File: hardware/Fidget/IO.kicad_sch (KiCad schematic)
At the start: 16 parts

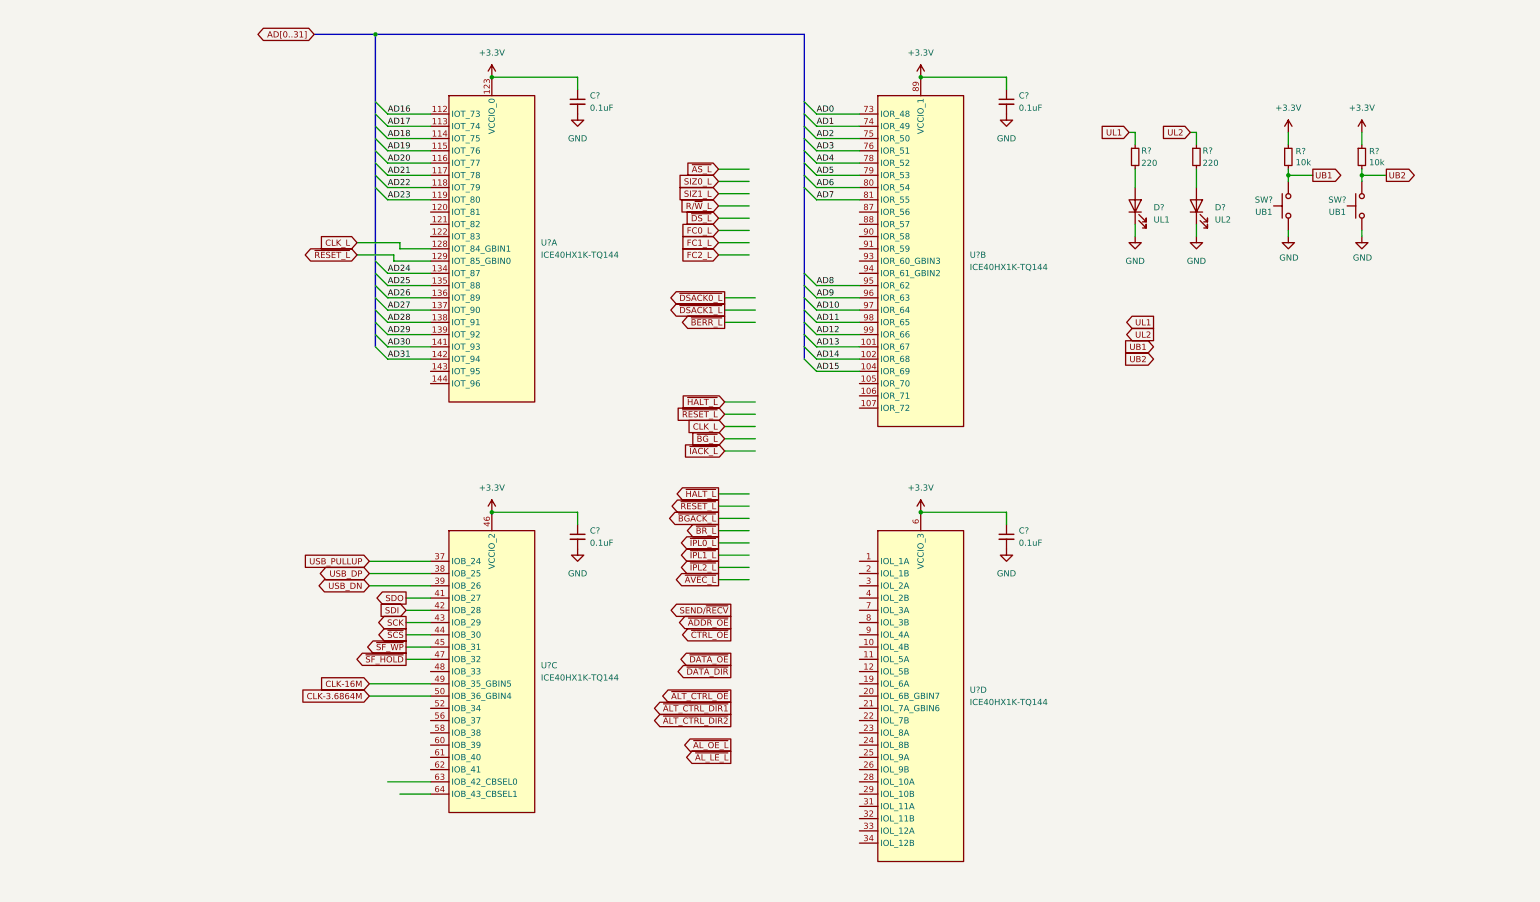
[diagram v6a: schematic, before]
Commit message: Minor updates, and start of PCB layout
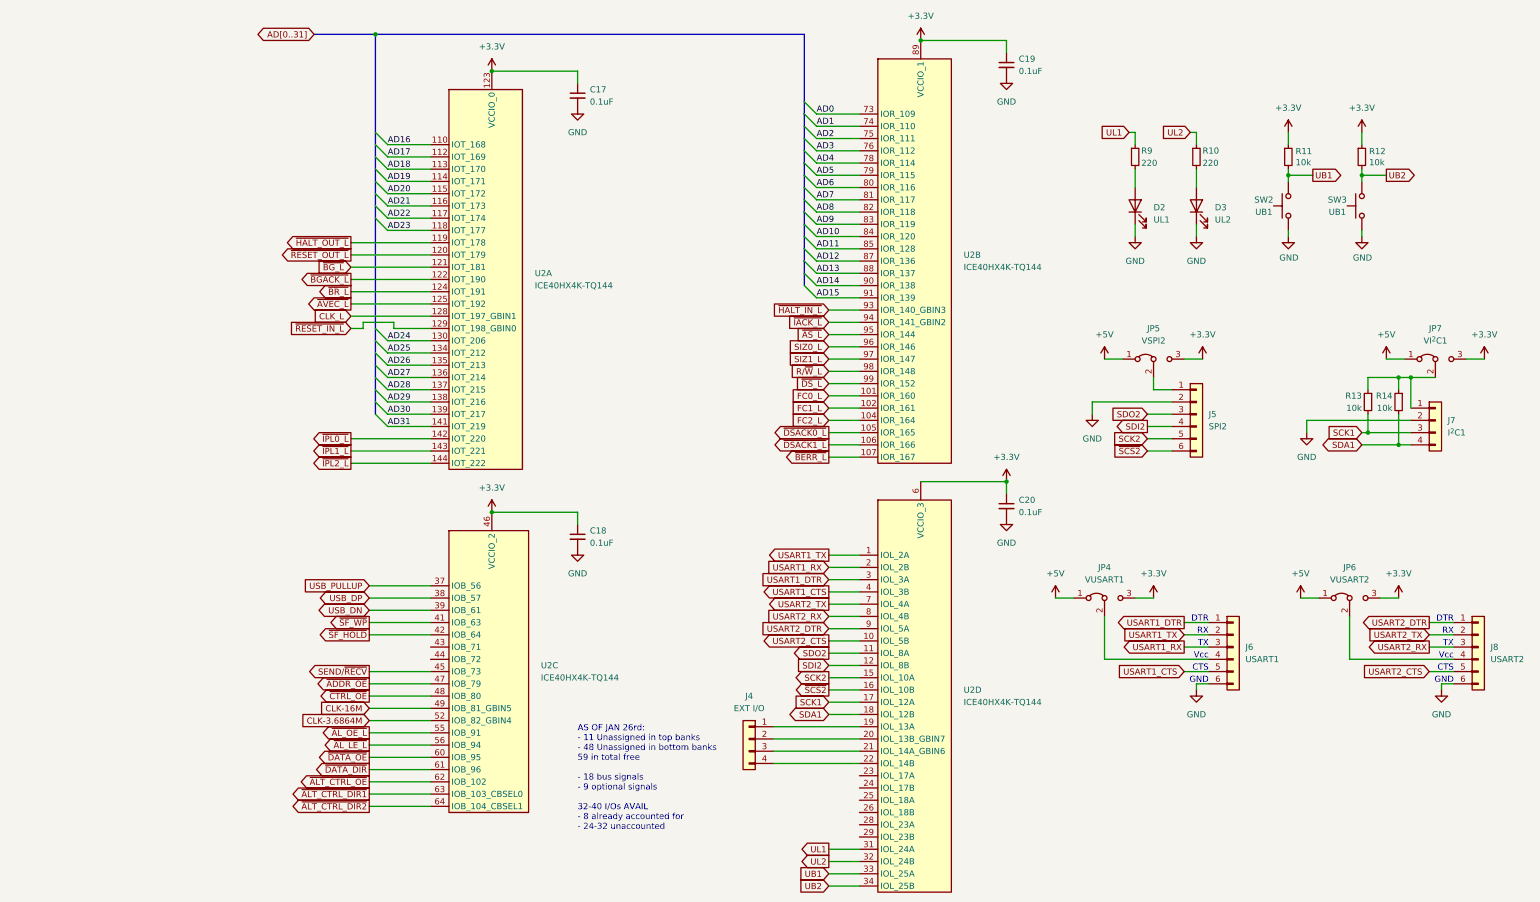
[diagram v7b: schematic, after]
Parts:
- removed U? (x4): ICE40HX1K-TQ144, Package_QFP:TQFP-144_20x20mm_P0.5mm, symbol FPGA_Lattice:ICE40HX1K-TQ144
- added J4: EXT I/O, Connector_PinHeader_2.54mm:PinHeader_1x04_P2.54mm_Vertical, symbol Connector_Generic:Conn_01x04
- added J5: SPI2, Connector_PinHeader_2.54mm:PinHeader_1x06_P2.54mm_Vertical, symbol Connector_Generic:Conn_01x06
- added J6: USART1, Connector_PinHeader_2.54mm:PinHeader_1x06_P2.54mm_Vertical, symbol Connector_Generic:Conn_01x06
- added J7: I^{2}C1, Connector_PinHeader_2.54mm:PinHeader_1x04_P2.54mm_Vertical, symbol Connector_Generic:Conn_01x04
- added J8: USART2, Connector_PinHeader_2.54mm:PinHeader_1x06_P2.54mm_Vertical, symbol Connector_Generic:Conn_01x06
- added JP4: VUSART1, Connector_PinHeader_2.54mm:PinHeader_1x03_P2.54mm_Vertical, symbol Jumper:Jumper_3_Bridged12
- added JP5: VSPI2, Connector_PinHeader_2.54mm:PinHeader_1x03_P2.54mm_Vertical, symbol Jumper:Jumper_3_Bridged12
- added JP6: VUSART2, Connector_PinHeader_2.54mm:PinHeader_1x03_P2.54mm_Vertical, symbol Jumper:Jumper_3_Bridged12
- added JP7: VI^{2}C1, Connector_PinHeader_2.54mm:PinHeader_1x03_P2.54mm_Vertical, symbol Jumper:Jumper_3_Bridged12
- added R13, R14: 10k, Resistor_THT:R_Axial_DIN0204_L3.6mm_D1.6mm_P5.08mm_Horizontal, symbol Device:R_Small
- added U2: ICE40HX4K-TQ144, Package_QFP:TQFP-144_20x20mm_P0.5mm, symbol FPGA_Lattice:ICE40HX4K-TQ144
- C17, C18, C19, C20: renamed from C?; footprint (none) -> Capacitor_SMD:C_0805_2012Metric_Pad1.18x1.45mm_HandSolder
- R10, R9: renamed from R?; footprint (none) -> Resistor_THT:R_Axial_DIN0204_L3.6mm_D1.6mm_P5.08mm_Horizontal
- gave numbers to parts that had none: 6
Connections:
- net +3.3V: now also JP4.3 (B), JP5.3 (B), JP6.3 (B), JP7.3 (B), U2.100 (VCCIO_1), U2.123 (VCCIO_0), U2.131 (VCCIO_0), U2.30 (VCCIO_3), U2.46 (VCCIO_2), U2.57 (VCCIO_2), U2.6 (VCCIO_3), U2.89 (VCCIO_1)
- net AD0: now also U2.73 (IOR_109)
- net AD1: now also U2.74 (IOR_110)
- net AD10: now also U2.84 (IOR_120)
- net AD11: now also U2.85 (IOR_128)
- net AD12: now also U2.87 (IOR_136)
- net AD13: now also U2.88 (IOR_137)
- net AD14: now also U2.90 (IOR_138)
- net AD15: now also U2.91 (IOR_139)
- net AD16: now also U2.110 (IOT_168)
- net AD17: now also U2.112 (IOT_169)
- net AD18: now also U2.113 (IOT_170)
- net AD19: now also U2.114 (IOT_171)
- net AD2: now also U2.75 (IOR_111)
- net AD20: now also U2.115 (IOT_172)
- net AD21: now also U2.116 (IOT_173)
- net AD22: now also U2.117 (IOT_174)
- net AD23: now also U2.118 (IOT_177)
- net AD24: now also U2.130 (IOT_206)
- net AD25: now also U2.134 (IOT_212)
- net AD26: now also U2.135 (IOT_213)
- net AD27: now also U2.136 (IOT_214)
- net AD28: now also U2.137 (IOT_215)
- net AD29: now also U2.138 (IOT_216)
- net AD3: now also U2.76 (IOR_112)
- net AD30: now also U2.139 (IOT_217)
- net AD31: now also U2.141 (IOT_219)
- net AD4: now also U2.78 (IOR_114)
- net AD5: now also U2.79 (IOR_115)
- net AD6: now also U2.80 (IOR_116)
- net AD7: now also U2.81 (IOR_117)
- net AD8: now also U2.82 (IOR_118)
- net AD9: now also U2.83 (IOR_119)
- net CLK-16M: now also U2.49 (IOB_81_GBIN5)
- net CLK-3.6864M: now also U2.52 (IOB_82_GBIN4)
- net CLK_L: now also U2.128 (IOT_197_GBIN1)
- net FC0_L: now also U2.101 (IOR_160)
- net FC1_L: now also U2.102 (IOR_161)
- net FC2_L: now also U2.104 (IOR_164)
- net GND: now also J5.2 (Pin_2), J6.6 (Pin_6), J7.2 (Pin_2), J8.6 (Pin_6)
- net R/~{W}_L: now also U2.98 (IOR_148)
- net SEND/~{RECV}: now also U2.45 (IOB_73)
- net SIZ0_L: now also U2.96 (IOR_146)
- net SIZ1_L: now also U2.97 (IOR_147)
- net UB1: now also U2.33 (IOL_25A)
- net UB2: now also U2.34 (IOL_25B)
- net UL1: now also U2.31 (IOL_24A)
- net UL2: now also U2.32 (IOL_24B)
- net USB_DN: now also U2.39 (IOB_61)
- net USB_DP: now also U2.38 (IOB_57)
- net USB_PULLUP: now also U2.37 (IOB_56)
- net ~{ADDR_OE}: now also U2.47 (IOB_79)
- net ~{ALT_CTRL_DIR1}: now also U2.63 (IOB_103_CBSEL0)
- net ~{ALT_CTRL_DIR2}: now also U2.64 (IOB_104_CBSEL1)
- net ~{ALT_CTRL_OE}: now also U2.62 (IOB_102)
- net ~{AL_LE_L}: now also U2.56 (IOB_94)
- net ~{AL_OE_L}: now also U2.55 (IOB_91)
- net ~{AS_L}: now also U2.95 (IOR_144)
- net ~{AVEC_L}: now also U2.125 (IOT_192)
- net ~{BERR_L}: now also U2.107 (IOR_167)
- net ~{BGACK_L}: now also U2.122 (IOT_190)
- net ~{BG_L}: now also U2.121 (IOT_181)
- net ~{BR_L}: now also U2.124 (IOT_191)
- net ~{CTRL_OE}: now also U2.48 (IOB_80)
- net ~{DATA_DIR}: now also U2.61 (IOB_96)
- net ~{DATA_OE}: now also U2.60 (IOB_95)
- net ~{DSACK0_L}: now also U2.105 (IOR_165)
- net ~{DSACK1_L}: now also U2.106 (IOR_166)
- net ~{DS_L}: now also U2.99 (IOR_152)
- net ~{IACK_L}: now also U2.94 (IOR_141_GBIN2)
- net ~{IPL0_L}: now also U2.142 (IOT_220)
- net ~{IPL1_L}: now also U2.143 (IOT_221)
- net ~{IPL2_L}: now also U2.144 (IOT_222)
- net ~{SF_HOLD}: now also U2.42 (IOB_64)
- net ~{SF_WP}: now also U2.41 (IOB_63)
- new net: J5.1 (Pin_1), JP5.2 (C)
- new net: J6.4 (Pin_4), JP4.2 (C)
- new net: J4.1 (Pin_1), U2.19 (IOL_13A)
- new net: J4.2 (Pin_2), U2.20 (IOL_13B_GBIN7)
- new net: J4.3 (Pin_3), U2.21 (IOL_14A_GBIN6)
- new net: J4.4 (Pin_4), U2.22 (IOL_14B)
- new net: J8.4 (Pin_4), JP6.2 (C)
- new net: J7.1 (Pin_1), JP7.2 (C), R13.1, R14.1
- new net +5V: JP4.1 (A), JP5.1 (A), JP6.1 (A), JP7.1 (A)
- new net SCK1: J7.3 (Pin_3), R13.2, U2.17 (IOL_12A)
- new net SCK2: J5.5 (Pin_5), U2.15 (IOL_10A)
- new net SDA1: J7.4 (Pin_4), R14.2, U2.18 (IOL_12B)
- new net SDI2: J5.4 (Pin_4), U2.12 (IOL_8B)
- new net SDO2: J5.3 (Pin_3), U2.11 (IOL_8A)
- new net USART1_CTS: J6.5 (Pin_5), U2.4 (IOL_3B)
- new net USART1_DTR: J6.1 (Pin_1), U2.3 (IOL_3A)
- new net USART1_RX: J6.3 (Pin_3), U2.2 (IOL_2B)
- new net USART1_TX: J6.2 (Pin_2), U2.1 (IOL_2A)
- new net USART2_CTS: J8.5 (Pin_5), U2.10 (IOL_5B)
- new net USART2_DTR: J8.1 (Pin_1), U2.9 (IOL_5A)
- new net USART2_RX: J8.3 (Pin_3), U2.8 (IOL_4B)
- new net USART2_TX: J8.2 (Pin_2), U2.7 (IOL_4A)
- new net ~{HALT_IN_L}: U2.93 (IOR_140_GBIN3)
- new net ~{HALT_OUT_L}: U2.119 (IOT_178)
- new net ~{RESET_IN_L}: U2.129 (IOT_198_GBIN0)
- new net ~{RESET_OUT_L}: U2.120 (IOT_179)
- new net ~{SCS2}: J5.6 (Pin_6), U2.16 (IOL_10B)
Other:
- note added: "AS OF JAN 26rd: - 11 Unassigned in top banks - 48 Unassigned in bottom banks 59 in total free - 18 bus signals - 9 optional signals 32-40 I/Os AVAIL - 8 already accounted for - 24-32 unaccounted"
- note added: "CTS"
- note added: "DTR"
- note added: "GND"
- note added: "RX"
- note added: "TX"
- note added: "Vcc"
- moved on the sheet: C17, C19, C20

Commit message: More PCB layout and fixes and reassigments to the schematics
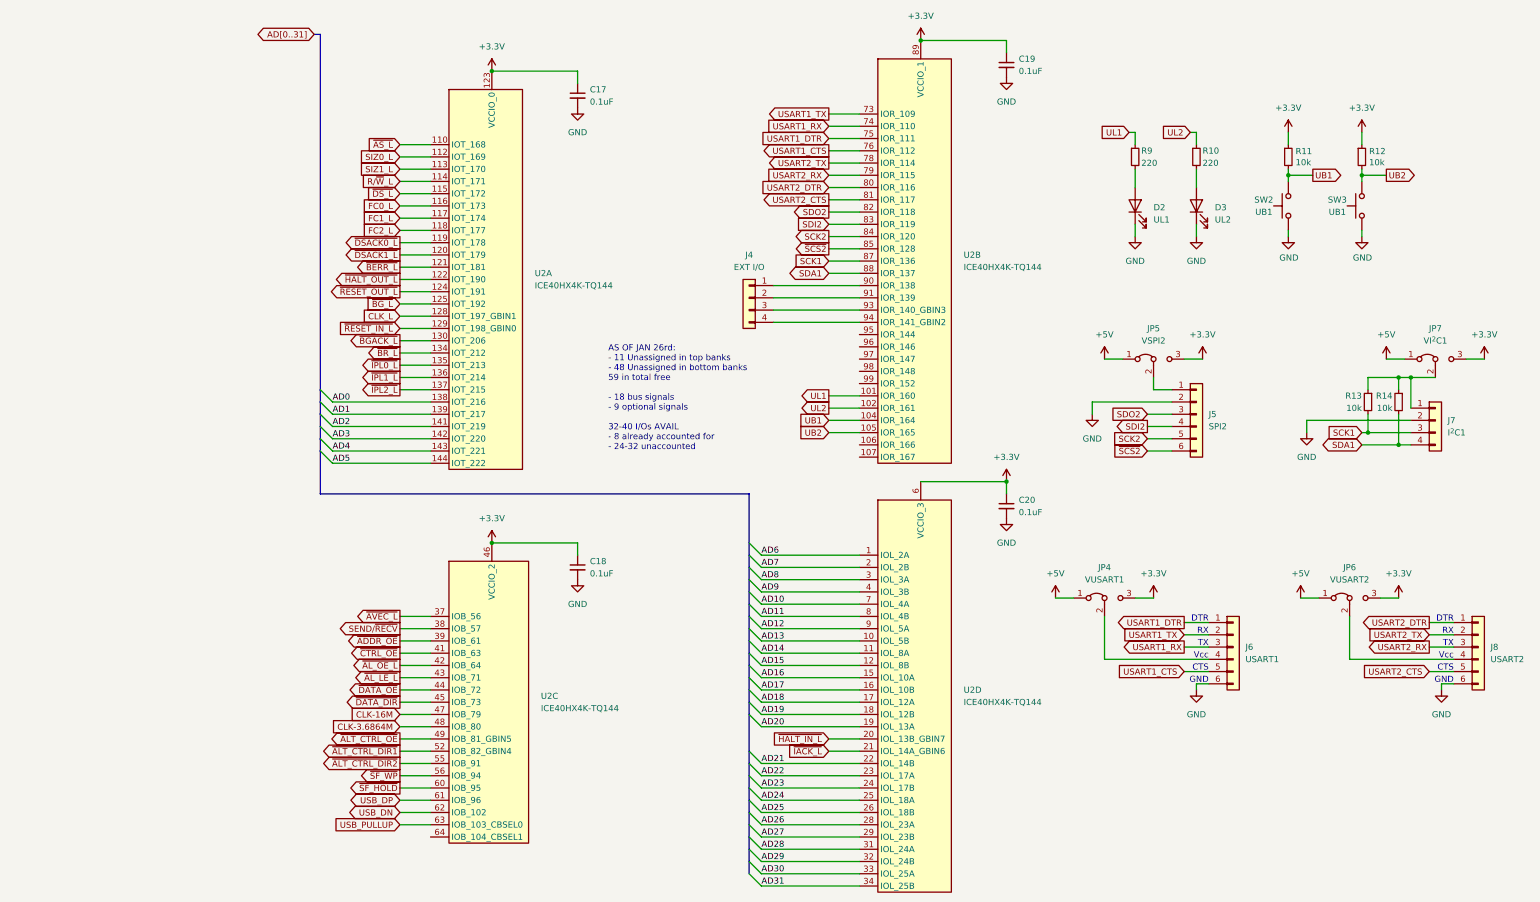
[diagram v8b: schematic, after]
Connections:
- net AD0: now also U2.138 (IOT_216); no longer U2.73 (IOR_109)
- net AD1: now also U2.139 (IOT_217); no longer U2.74 (IOR_110)
- net AD10: now also U2.7 (IOL_4A); no longer U2.84 (IOR_120)
- net AD11: now also U2.8 (IOL_4B); no longer U2.85 (IOR_128)
- net AD12: now also U2.9 (IOL_5A); no longer U2.87 (IOR_136)
- net AD13: now also U2.10 (IOL_5B); no longer U2.88 (IOR_137)
- net AD14: now also U2.11 (IOL_8A); no longer U2.90 (IOR_138)
- net AD15: now also U2.12 (IOL_8B); no longer U2.91 (IOR_139)
- net AD16: now also U2.15 (IOL_10A); no longer U2.110 (IOT_168)
- net AD17: now also U2.16 (IOL_10B); no longer U2.112 (IOT_169)
- net AD18: now also U2.17 (IOL_12A); no longer U2.113 (IOT_170)
- net AD19: now also U2.18 (IOL_12B); no longer U2.114 (IOT_171)
- net AD2: now also U2.141 (IOT_219); no longer U2.75 (IOR_111)
- net AD20: now also U2.19 (IOL_13A); no longer U2.115 (IOT_172)
- net AD21: now also U2.22 (IOL_14B); no longer U2.116 (IOT_173)
- net AD22: now also U2.23 (IOL_17A); no longer U2.117 (IOT_174)
- net AD23: now also U2.24 (IOL_17B); no longer U2.118 (IOT_177)
- net AD24: now also U2.25 (IOL_18A); no longer U2.130 (IOT_206)
- net AD25: now also U2.26 (IOL_18B); no longer U2.134 (IOT_212)
- net AD26: now also U2.28 (IOL_23A); no longer U2.135 (IOT_213)
- net AD27: now also U2.29 (IOL_23B); no longer U2.136 (IOT_214)
- net AD28: now also U2.31 (IOL_24A); no longer U2.137 (IOT_215)
- net AD29: now also U2.32 (IOL_24B); no longer U2.138 (IOT_216)
- net AD3: now also U2.142 (IOT_220); no longer U2.76 (IOR_112)
- net AD30: now also U2.33 (IOL_25A); no longer U2.139 (IOT_217)
- net AD31: now also U2.34 (IOL_25B); no longer U2.141 (IOT_219)
- net AD4: now also U2.143 (IOT_221); no longer U2.78 (IOR_114)
- net AD5: now also U2.144 (IOT_222); no longer U2.79 (IOR_115)
- net AD6: now also U2.1 (IOL_2A); no longer U2.80 (IOR_116)
- net AD7: now also U2.2 (IOL_2B); no longer U2.81 (IOR_117)
- net AD8: now also U2.3 (IOL_3A); no longer U2.82 (IOR_118)
- net AD9: now also U2.4 (IOL_3B); no longer U2.83 (IOR_119)
- net CLK-16M: now also U2.47 (IOB_79); no longer U2.49 (IOB_81_GBIN5)
- net CLK-3.6864M: now also U2.48 (IOB_80); no longer U2.52 (IOB_82_GBIN4)
- net FC0_L: now also U2.116 (IOT_173); no longer U2.101 (IOR_160)
- net FC1_L: now also U2.117 (IOT_174); no longer U2.102 (IOR_161)
- net FC2_L: now also U2.118 (IOT_177); no longer U2.104 (IOR_164)
- net R/~{W}_L: now also U2.114 (IOT_171); no longer U2.98 (IOR_148)
- net SCK1: now also U2.87 (IOR_136); no longer U2.17 (IOL_12A)
- net SCK2: now also U2.84 (IOR_120); no longer U2.15 (IOL_10A)
- net SDA1: now also U2.88 (IOR_137); no longer U2.18 (IOL_12B)
- net SDI2: now also U2.83 (IOR_119); no longer U2.12 (IOL_8B)
- net SDO2: now also U2.82 (IOR_118); no longer U2.11 (IOL_8A)
- net SEND/~{RECV}: now also U2.38 (IOB_57); no longer U2.45 (IOB_73)
- net SIZ0_L: now also U2.112 (IOT_169); no longer U2.96 (IOR_146)
- net SIZ1_L: now also U2.113 (IOT_170); no longer U2.97 (IOR_147)
- net UB1: now also U2.104 (IOR_164); no longer U2.33 (IOL_25A)
- net UB2: now also U2.105 (IOR_165); no longer U2.34 (IOL_25B)
- net UL1: now also U2.101 (IOR_160); no longer U2.31 (IOL_24A)
- net UL2: now also U2.102 (IOR_161); no longer U2.32 (IOL_24B)
- net USART1_CTS: now also U2.76 (IOR_112); no longer U2.4 (IOL_3B)
- net USART1_DTR: now also U2.75 (IOR_111); no longer U2.3 (IOL_3A)
- net USART1_RX: now also U2.74 (IOR_110); no longer U2.2 (IOL_2B)
- net USART1_TX: now also U2.73 (IOR_109); no longer U2.1 (IOL_2A)
- net USART2_CTS: now also U2.81 (IOR_117); no longer U2.10 (IOL_5B)
- net USART2_DTR: now also U2.80 (IOR_116); no longer U2.9 (IOL_5A)
- net USART2_RX: now also U2.79 (IOR_115); no longer U2.8 (IOL_4B)
- net USART2_TX: now also U2.78 (IOR_114); no longer U2.7 (IOL_4A)
- net USB_DN: now also U2.62 (IOB_102); no longer U2.39 (IOB_61)
- net USB_DP: now also U2.61 (IOB_96); no longer U2.38 (IOB_57)
- net USB_PULLUP: now also U2.63 (IOB_103_CBSEL0); no longer U2.37 (IOB_56)
- net ~{ADDR_OE}: now also U2.39 (IOB_61); no longer U2.47 (IOB_79)
- net ~{ALT_CTRL_DIR1}: now also U2.52 (IOB_82_GBIN4); no longer U2.63 (IOB_103_CBSEL0)
- net ~{ALT_CTRL_DIR2}: now also U2.55 (IOB_91); no longer U2.64 (IOB_104_CBSEL1)
- net ~{ALT_CTRL_OE}: now also U2.49 (IOB_81_GBIN5); no longer U2.62 (IOB_102)
- net ~{AL_LE_L}: now also U2.43 (IOB_71); no longer U2.56 (IOB_94)
- net ~{AL_OE_L}: now also U2.42 (IOB_64); no longer U2.55 (IOB_91)
- net ~{AS_L}: now also U2.110 (IOT_168); no longer U2.95 (IOR_144)
- net ~{AVEC_L}: now also U2.37 (IOB_56); no longer U2.125 (IOT_192)
- net ~{BERR_L}: now also U2.121 (IOT_181); no longer U2.107 (IOR_167)
- net ~{BGACK_L}: now also U2.130 (IOT_206); no longer U2.122 (IOT_190)
- net ~{BG_L}: now also U2.125 (IOT_192); no longer U2.121 (IOT_181)
- net ~{BR_L}: now also U2.134 (IOT_212); no longer U2.124 (IOT_191)
- net ~{CTRL_OE}: now also U2.41 (IOB_63); no longer U2.48 (IOB_80)
- net ~{DATA_DIR}: now also U2.45 (IOB_73); no longer U2.61 (IOB_96)
- net ~{DATA_OE}: now also U2.44 (IOB_72); no longer U2.60 (IOB_95)
- net ~{DSACK0_L}: now also U2.119 (IOT_178); no longer U2.105 (IOR_165)
- net ~{DSACK1_L}: now also U2.120 (IOT_179); no longer U2.106 (IOR_166)
- net ~{DS_L}: now also U2.115 (IOT_172); no longer U2.99 (IOR_152)
- net ~{HALT_IN_L}: now also U2.20 (IOL_13B_GBIN7); no longer U2.93 (IOR_140_GBIN3)
- net ~{HALT_OUT_L}: now also U2.122 (IOT_190); no longer U2.119 (IOT_178)
- net ~{IACK_L}: now also U2.21 (IOL_14A_GBIN6); no longer U2.94 (IOR_141_GBIN2)
- net ~{IPL0_L}: now also U2.135 (IOT_213); no longer U2.142 (IOT_220)
- net ~{IPL1_L}: now also U2.136 (IOT_214); no longer U2.143 (IOT_221)
- net ~{IPL2_L}: now also U2.137 (IOT_215); no longer U2.144 (IOT_222)
- net ~{RESET_OUT_L}: now also U2.124 (IOT_191); no longer U2.120 (IOT_179)
- net ~{SCS2}: now also U2.85 (IOR_128); no longer U2.16 (IOL_10B)
- net ~{SF_HOLD}: now also U2.60 (IOB_95); no longer U2.42 (IOB_64)
- net ~{SF_WP}: now also U2.56 (IOB_94); no longer U2.41 (IOB_63)
- net at J4.1 (Pin_1): now also U2.90 (IOR_138); no longer U2.19 (IOL_13A)
- net at J4.2 (Pin_2): now also U2.91 (IOR_139); no longer U2.20 (IOL_13B_GBIN7)
- net at J4.3 (Pin_3): now also U2.93 (IOR_140_GBIN3); no longer U2.21 (IOL_14A_GBIN6)
- net at J4.4 (Pin_4): now also U2.94 (IOR_141_GBIN2); no longer U2.22 (IOL_14B)
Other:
- moved on the sheet: C18, J4, U2C
